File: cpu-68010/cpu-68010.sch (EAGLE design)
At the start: 86 parts, among them IC10 74HC30D, IC11 74HC30D, IC12 74HC14D, IC13 MAX232, IC6 74HC00D, IC7 74HCT154DW, IC8 74HC04D, IC9 74HC148D, Q1 3.6864MHz, X1 FABC96R

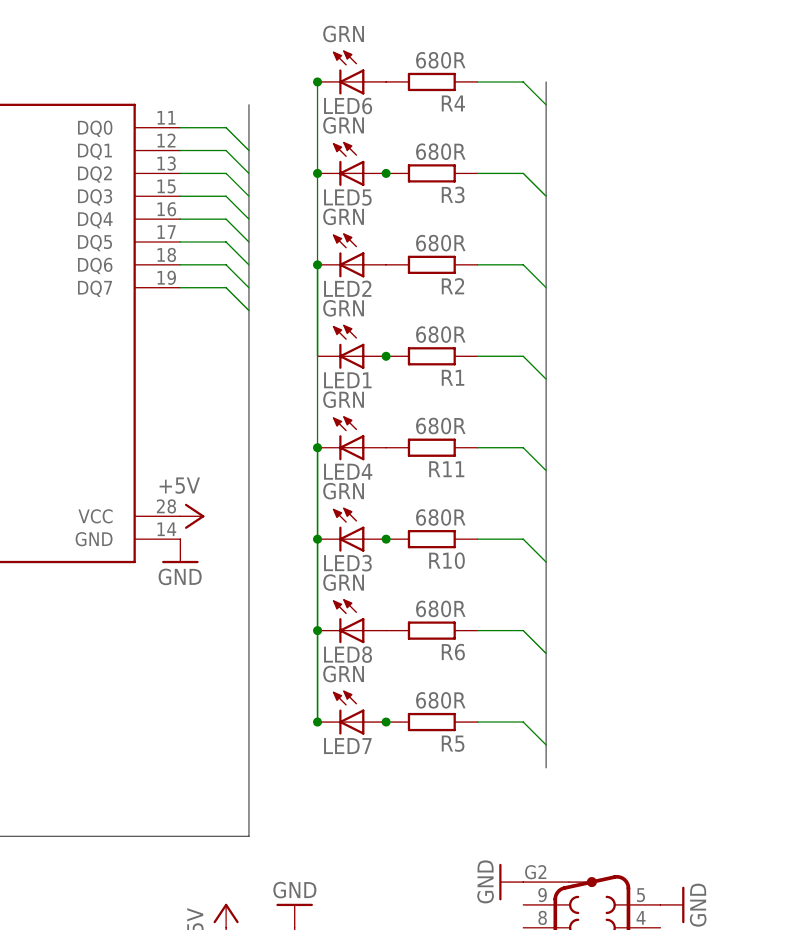
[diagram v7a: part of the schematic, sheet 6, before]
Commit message: routed address/data between banks of RAM/ROM
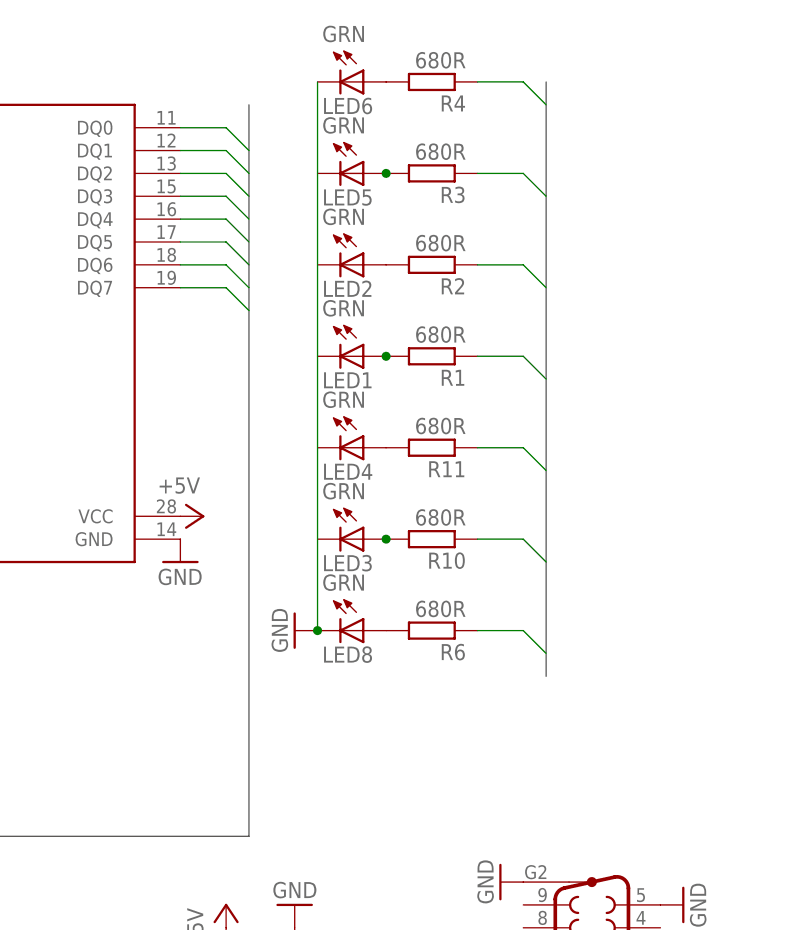
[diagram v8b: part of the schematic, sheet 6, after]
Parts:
- removed LED7: GRN, led:LEDCHIPLED_1206
- removed R5: 680R, rcl:R-EU_M0805
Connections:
- removed net GPIO_OUT7: IC2.OP7, R5.1
- removed net N$12: LED1.C, LED2.C
- removed net N$15: LED3.C, LED4.C, LED5.C, LED6.C, LED7.C, LED8.C
- removed net N$16: LED7.A, R5.2
- new net TIMER_CLK: IC2.OP2
- net GND: now also LED6.C, LED8.C
- net GPIO_OUT2: now also IC2.OP3; no longer IC2.OP2
- net GPIO_OUT3: now also IC2.OP4; no longer IC2.OP3
- net GPIO_OUT4: now also IC2.OP5; no longer IC2.OP4
- net GPIO_OUT5: now also IC2.OP6; no longer IC2.OP5
- net GPIO_OUT6: now also IC2.OP7; no longer IC2.OP6
- net R!W!: no longer IC2.R/!W, IC5.!WE
- net R/!W!: now also IC2.R/!W, IC5.!WE
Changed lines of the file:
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@@
 <attribute name="MOUSER" value="604-APTR3216SGC"/>
 </part>
-<part name="LED7" library="led" library_urn="urn:adsk.eagle:library:259" deviceset="LED" device="CHIPLED_1206" package3d_urn="urn:adsk.eagle:package:15823/2" value="GRN">
-<attribute name="MOUSER" value="604-APTR3216SGC"/>
-</part>
-<part name="R5" library="rcl" library_urn="urn:adsk.eagle:library:334" deviceset="R-EU_" device="M0805" package3d_urn="urn:adsk.eagle:package:23556/1" value="680R">
-<attribute name="MOUSER" value="652-CR0805-FX6800GLF"/>
-</part>
 <part name="R6" library="rcl" library_urn="urn:adsk.eagle:library:334" deviceset="R-EU_" device="M0805" package3d_urn="urn:adsk.eagle:package:23556/1" value="680R">
 <attribute name="MOUSER" value="652-CR0805-FX6800GLF"/>
@@
 <part name="P+29" library="supply1" library_urn="urn:adsk.eagle:library:371" deviceset="+5V" device=""/>
 <part name="GND39" library="supply1" library_urn="urn:adsk.eagle:library:371" deviceset="GND" device=""/>
+<part name="GND40" library="supply1" library_urn="urn:adsk.eagle:library:371" deviceset="GND" device=""/>
 </parts>
 <sheets>
@@
 <attribute name="VALUE" x="119.888" y="182.245" size="1.778" layer="96"/>
 </instance>
-<instance part="LED7" gate="G$1" x="124.46" y="106.68" smashed="yes" rot="R270">
-<attribute name="MOUSER" x="124.46" y="106.68" size="1.27" layer="96" rot="R270" align="top-center" display="off"/>
-<attribute name="NAME" x="119.888" y="103.124" size="1.778" layer="95"/>
-<attribute name="VALUE" x="119.888" y="111.125" size="1.778" layer="96"/>
-</instance>
-<instance part="R5" gate="G$1" x="132.08" y="106.68" smashed="yes" rot="R180">
-<attribute name="MOUSER" x="132.08" y="106.68" size="1.27" layer="96" rot="R180" align="top-center" display="off"/>
-<attribute name="NAME" x="135.89" y="105.1814" size="1.778" layer="95" rot="R180"/>
-<attribute name="VALUE" x="135.89" y="109.982" size="1.778" layer="96" rot="R180"/>
-</instance>
 <instance part="R6" gate="G$1" x="132.08" y="116.84" smashed="yes" rot="R180">
 <attribute name="MOUSER" x="132.08" y="116.84" size="1.27" layer="96" rot="R180" align="top-center" display="off"/>
@@
 <attribute name="VALUE" x="162.56" y="58.42" size="1.778" layer="96" rot="R90"/>
 </instance>
+<instance part="GND40" gate="1" x="116.84" y="116.84" smashed="yes" rot="R270">
+<attribute name="VALUE" x="114.3" y="119.38" size="1.778" layer="96" rot="R270"/>
+</instance>
 </instances>
 <busses>
-<bus name="!68681_CS,!68681_DTACK,!68681_IACK,!68681_IRQ,!68681_IRQACK,68681_XTAL[1..2],A[1..23],CLK,D[0..15],GPIO_IN[0..5],GPIO_OUT[0..7],!LDS,!OE,!RESET,!RTC_CS,R!W!,UART0_RX,UART0_TX,UART1_RX,UART1_TX">
+<bus name="!68681_CS,!68681_DTACK,!68681_IACK,!68681_IRQ,!68681_IRQACK,68681_XTAL[1..2],A[1..23],CLK,D[0..15],GPIO_IN[0..5],GPIO_OUT[0..6],!LDS,!OE,!RESET,!RTC_CS,R!W!,TIMER_CLK,UART0_RX,UART0_TX,UART1_RX,UART1_TX">
 <segment>
 <wire x1="7.62" y1="175.26" x2="7.62" y2="93.98" width="0.762" layer="92"/>
@@
 <bus name="GPIO_OUT[0..7]">
 <segment>
-<wire x1="144.78" y1="177.8" x2="144.78" y2="101.6" width="0.762" layer="92"/>
+<wire x1="144.78" y1="177.8" x2="144.78" y2="111.76" width="0.762" layer="92"/>
 </segment>
 </bus>
@@
 <pinref part="GND31" gate="1" pin="GND"/>
 </segment>
+<segment>
+<pinref part="LED8" gate="G$1" pin="C"/>
+<pinref part="GND40" gate="1" pin="GND"/>
+<pinref part="LED6" gate="G$1" pin="C"/>
+<wire x1="119.38" y1="116.84" x2="119.38" y2="177.8" width="0.1524" layer="91"/>
+<junction x="119.38" y="116.84"/>
+</segment>
 </net>
-<net name="R!W!" class="0">
+<net name="R/!W!" class="0">
 <segment>
 <pinref part="IC5" gate="G$1" pin="!WE"/>
@@
 <net name="GPIO_OUT2" class="0">
 <segment>
-<pinref part="IC2" gate="G$1" pin="OP2"/>
-<wire x1="45.72" y1="149.86" x2="50.8" y2="149.86" width="0.1524" layer="91"/>
-<wire x1="50.8" y1="149.86" x2="53.34" y2="147.32" width="0.1524" layer="91"/>
-</segment>
-<segment>
 <pinref part="R2" gate="G$1" pin="1"/>
 <wire x1="137.16" y1="157.48" x2="142.24" y2="157.48" width="0.1524" layer="91"/>
 <wire x1="142.24" y1="157.48" x2="144.78" y2="154.94" width="0.1524" layer="91"/>
 </segment>
-</net>
-<net name="GPIO_OUT3" class="0">
 <segment>
 <pinref part="IC2" gate="G$1" pin="OP3"/>
@@
 <wire x1="50.8" y1="147.32" x2="53.34" y2="144.78" width="0.1524" layer="91"/>
 </segment>
+</net>
+<net name="GPIO_OUT3" class="0">
 <segment>
 <pinref part="R1" gate="G$1" pin="1"/>
@@
 <wire x1="142.24" y1="147.32" x2="144.78" y2="144.78" width="0.1524" layer="91"/>
 </segment>
-</net>
-<net name="GPIO_OUT4" class="0">
 <segment>
 <pinref part="IC2" gate="G$1" pin="OP4"/>
@@
 <wire x1="50.8" y1="144.78" x2="53.34" y2="142.24" width="0.1524" layer="91"/>
 </segment>
+</net>
+<net name="GPIO_OUT4" class="0">
 <segment>
 <pinref part="R11" gate="G$1" pin="1"/>
@@
 <wire x1="142.24" y1="137.16" x2="144.78" y2="134.62" width="0.1524" layer="91"/>
 </segment>
-</net>
-<net name="GPIO_OUT5" class="0">
 <segment>
 <pinref part="IC2" gate="G$1" pin="OP5"/>
@@
 <wire x1="50.8" y1="142.24" x2="53.34" y2="139.7" width="0.1524" layer="91"/>
 </segment>
+</net>
+<net name="GPIO_OUT5" class="0">
 <segment>
 <pinref part="R10" gate="G$1" pin="1"/>
@@
 <wire x1="142.24" y1="127" x2="144.78" y2="124.46" width="0.1524" layer="91"/>
 </segment>
-</net>
-<net name="GPIO_OUT6" class="0">
 <segment>
 <pinref part="IC2" gate="G$1" pin="OP6"/>
@@
 <wire x1="50.8" y1="139.7" x2="53.34" y2="137.16" width="0.1524" layer="91"/>
 </segment>
+</net>
+<net name="GPIO_OUT6" class="0">
 <segment>
 <pinref part="R6" gate="G$1" pin="1"/>
@@
 <wire x1="142.24" y1="116.84" x2="144.78" y2="114.3" width="0.1524" layer="91"/>
 </segment>
-</net>
-<net name="GPIO_OUT7" class="0">
 <segment>
 <pinref part="IC2" gate="G$1" pin="OP7"/>
@@
 <wire x1="50.8" y1="137.16" x2="53.34" y2="134.62" width="0.1524" layer="91"/>
 </segment>
-<segment>
-<pinref part="R5" gate="G$1" pin="1"/>
-<wire x1="137.16" y1="106.68" x2="142.24" y2="106.68" width="0.1524" layer="91"/>
-<wire x1="142.24" y1="106.68" x2="144.78" y2="104.14" width="0.1524" layer="91"/>
-</segment>
 </net>
 <net name="68681_XTAL2" class="0">
@@
 </segment>
 </net>
-<net name="N$12" class="0">
-<segment>
-<pinref part="LED1" gate="G$1" pin="C"/>
-<pinref part="LED2" gate="G$1" pin="C"/>
-<wire x1="119.38" y1="147.32" x2="119.38" y2="157.48" width="0.1524" layer="91"/>
-<junction x="119.38" y="157.48"/>
-</segment>
-</net>
 <net name="N$13" class="0">
 <segment>
@@
 </segment>
 </net>
-<net name="N$15" class="0">
-<segment>
-<pinref part="LED5" gate="G$1" pin="C"/>
-<pinref part="LED6" gate="G$1" pin="C"/>
-<wire x1="119.38" y1="167.64" x2="119.38" y2="177.8" width="0.1524" layer="91"/>
-<junction x="119.38" y="177.8"/>
-<pinref part="LED7" gate="G$1" pin="C"/>
-<pinref part="LED8" gate="G$1" pin="C"/>
-<wire x1="119.38" y1="106.68" x2="119.38" y2="116.84" width="0.1524" layer="91"/>
-<junction x="119.38" y="116.84"/>
-<pinref part="LED3" gate="G$1" pin="C"/>
-<pinref part="LED4" gate="G$1" pin="C"/>
-<wire x1="119.38" y1="127" x2="119.38" y2="137.16" width="0.1524" layer="91"/>
-<junction x="119.38" y="137.16"/>
-<wire x1="119.38" y1="116.84" x2="119.38" y2="127" width="0.1524" layer="91"/>
-<junction x="119.38" y="127"/>
-<wire x1="119.38" y1="167.64" x2="119.38" y2="106.68" width="0.1524" layer="91"/>
-<junction x="119.38" y="167.64"/>
-<junction x="119.38" y="106.68"/>
-</segment>
-</net>
-<net name="N$16" class="0">
-<segment>
-<pinref part="LED7" gate="G$1" pin="A"/>
-<pinref part="R5" gate="G$1" pin="2"/>
-<junction x="127" y="106.68"/>
-</segment>
-</net>
 <net name="N$17" class="0">
 <segment>
@@
 </segment>
 </net>
+<net name="TIMER_CLK" class="0">
+<segment>
+<pinref part="IC2" gate="G$1" pin="OP2"/>
+<wire x1="45.72" y1="149.86" x2="50.8" y2="149.86" width="0.1524" layer="91"/>
+<wire x1="50.8" y1="149.86" x2="53.34" y2="147.32" width="0.1524" layer="91"/>
+</segment>
+</net>
